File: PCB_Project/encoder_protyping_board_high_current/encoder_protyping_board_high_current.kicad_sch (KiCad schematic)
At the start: 15 parts, among them J1 Conn_01x08, J2 Conn_01x02_Pin, J3 Conn_01x04_Pin

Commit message: high current version done
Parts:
- JP1: footprint Jumper:SolderJumper-3_P1.3mm_Open_RoundedPad1.0x1.5mm -> Jumper:SolderJumper-3_P1.3mm_Open_RoundedPad1.0x1.5mm_NumberLabels
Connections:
- net GND: no longer J1.7 (Pin_7), U1.2 (P1)
- new net: J1.7 (Pin_7), U1.2 (P1)
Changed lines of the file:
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@@
-	)
-	(junction
-		(at 148.59 72.39)
-		(diameter 0)
-		(color 0 0 0 0)
 	)
 	(junction
@@
 	(wire
 		(pts
+			(xy 130.81 72.39) (xy 115.57 72.39)
+		)
+		(stroke
+			(width 0)
+			(type default)
+		)
+	)
+	(wire
+		(pts
 			(xy 182.88 115.57) (xy 166.37 115.57)
 		)
@@
 	(wire
 		(pts
-			(xy 158.75 64.77) (xy 215.9 64.77)
-		)
-		(stroke
-			(width 0)
-			(type default)
-		)
-	)
-	(wire
-		(pts
-			(xy 148.59 72.39) (xy 158.75 72.39)
-		)
-		(stroke
-			(width 0)
-			(type default)
-		)
-	)
-	(wire
-		(pts
 			(xy 74.93 83.82) (xy 92.71 83.82)
 		)
@@
 	(wire
 		(pts
+			(xy 115.57 69.85) (xy 129.54 69.85)
+		)
+		(stroke
+			(width 0)
+			(type default)
+		)
+	)
+	(wire
+		(pts
 			(xy 66.04 90.17) (xy 69.85 90.17)
 		)
@@
 	(wire
 		(pts
+			(xy 129.54 62.23) (xy 217.17 62.23)
+		)
+		(stroke
+			(width 0)
+			(type default)
+		)
+	)
+	(wire
+		(pts
 			(xy 148.59 120.65) (xy 143.51 120.65)
 		)
@@
 	(wire
 		(pts
-			(xy 115.57 72.39) (xy 148.59 72.39)
-		)
-		(stroke
-			(width 0)
-			(type default)
-		)
-	)
-	(wire
-		(pts
 			(xy 166.37 85.09) (xy 204.47 85.09)
 		)
@@
 	(wire
 		(pts
+			(xy 129.54 69.85) (xy 129.54 62.23)
+		)
+		(stroke
+			(width 0)
+			(type default)
+		)
+	)
+	(wire
+		(pts
 			(xy 74.93 86.36) (xy 92.71 86.36)
 		)
@@
 	(wire
 		(pts
-			(xy 158.75 72.39) (xy 158.75 64.77)
-		)
-		(stroke
-			(width 0)
-			(type default)
-		)
-	)
-	(wire
-		(pts
-			(xy 115.57 69.85) (xy 156.21 69.85)
+			(xy 130.81 64.77) (xy 130.81 72.39)
 		)
 		(stroke
@@
 	(wire
 		(pts
-			(xy 156.21 62.23) (xy 217.17 62.23)
-		)
-		(stroke
-			(width 0)
-			(type default)
-		)
-	)
-	(wire
-		(pts
 			(xy 69.85 90.17) (xy 76.2 90.17)
 		)
@@
 	(wire
 		(pts
+			(xy 130.81 64.77) (xy 215.9 64.77)
+		)
+		(stroke
+			(width 0)
+			(type default)
+		)
+	)
+	(wire
+		(pts
 			(xy 173.99 90.17) (xy 166.37 90.17)
 		)
@@
 		(pts
 			(xy 215.9 64.77) (xy 215.9 107.95)
-		)
-		(stroke
-			(width 0)
-			(type default)
-		)
-	)
-	(wire
-		(pts
-			(xy 156.21 69.85) (xy 156.21 62.23)
 		)
 		(stroke
@@
 			)
 		)
-		(property "Footprint" "Jumper:SolderJumper-3_P1.3mm_Open_RoundedPad1.0x1.5mm"
+		(property "Footprint" "Jumper:SolderJumper-3_P1.3mm_Open_RoundedPad1.0x1.5mm_NumberLabels"
 			(at 74.93 71.12 0)
 			(effects
@@
 	(symbol
 		(lib_id "power:GND")
-		(at 148.59 72.39 180)
+		(at 148.59 72.39 90)
 		(unit 1)
 		(exclude_from_sim no)
@@
 		(fields_autoplaced yes)
 		(property "Reference" "#PWR014"
-			(at 148.59 66.04 0)
+			(at 154.94 72.39 0)
 			(effects
 				(font
@@
 		)
 		(property "Value" "GND"
-			(at 148.59 67.31 0)
-			(effects
-				(font
-					(size 1.27 1.27)
-				)
-			)
-		)
+			(at 152.4 72.3899 90)
+			(effects
+				(font
+					(size 1.27 1.27)
+				)
+				(justify right)
+			)
+		)

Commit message: pin headers not pin sockets
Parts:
- J1: footprint Connector_PinSocket_2.54mm:PinSocket_1x08_P2.54mm_Vertical -> Connector_PinHeader_2.54mm:PinHeader_1x08_P2.54mm_Vertical
- J3: footprint Connector_PinSocket_2.54mm:PinSocket_1x04_P2.54mm_Vertical -> Connector_PinHeader_2.54mm:PinHeader_1x04_P2.54mm_Vertical
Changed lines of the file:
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@@
 			)
 		)
-		(property "Footprint" "Connector_PinSocket_2.54mm:PinSocket_1x04_P2.54mm_Vertical"
+		(property "Footprint" "Connector_PinHeader_2.54mm:PinHeader_1x04_P2.54mm_Vertical"
 			(at 88.9 41.91 0)
 			(effects
@@
 			)
 		)
-		(property "Footprint" "Connector_PinSocket_2.54mm:PinSocket_1x08_P2.54mm_Vertical"
+		(property "Footprint" "Connector_PinHeader_2.54mm:PinHeader_1x08_P2.54mm_Vertical"
 			(at 209.55 90.17 0)
 			(effects

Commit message: fixes
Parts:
- renumbered J2 to J1, J3 to J2, J1 to J3, JP2 to JP1, JP1 to JP2, R2 to R1, R3 to R2, R1 to R3
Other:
- moved on the sheet: R3

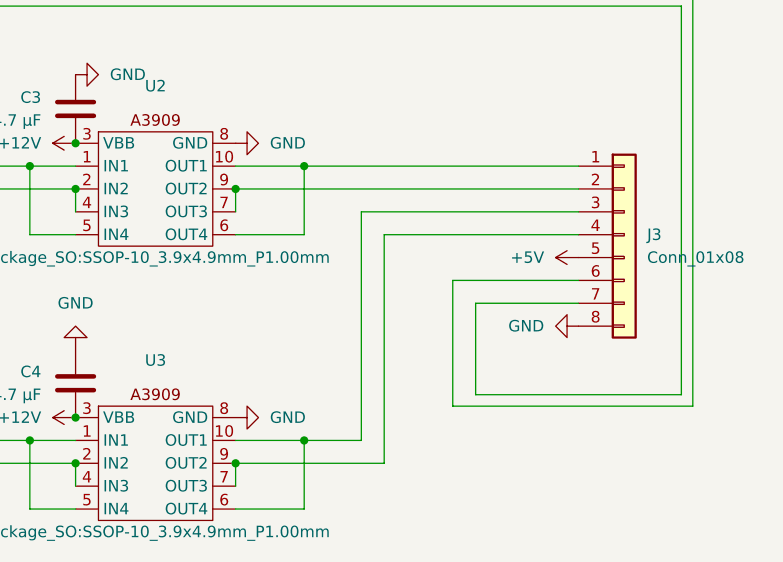
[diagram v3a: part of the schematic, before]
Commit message: finaly did that change to make it so this board could run with just a single chip
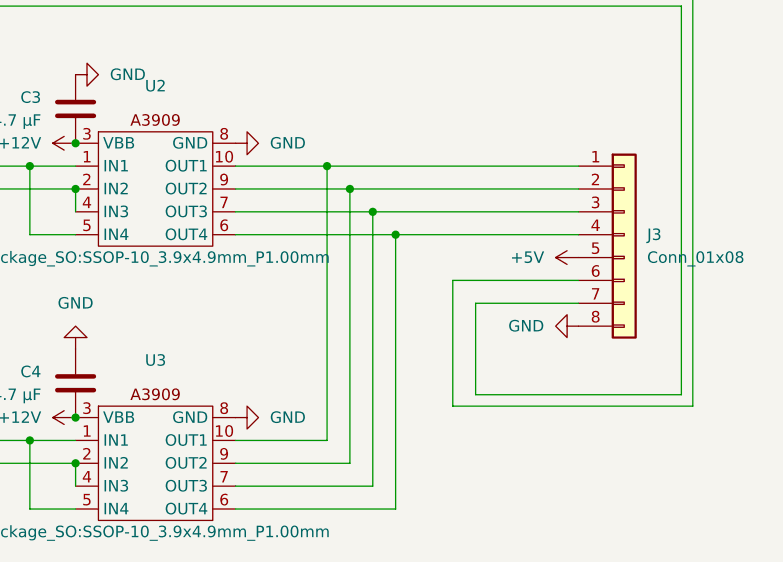
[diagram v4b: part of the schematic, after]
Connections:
- net at J3.1 (Pin_1), U2.10 (OUT1): now also U3.10 (OUT1); no longer U2.6 (OUT4)
- net at J3.2 (Pin_2), U2.9 (OUT2): now also U3.9 (OUT2); no longer U2.7 (OUT3)
- new net: J3.3 (Pin_3), U2.7 (OUT3), U3.7 (OUT3)
- new net: J3.4 (Pin_4), U2.6 (OUT4), U3.6 (OUT4)
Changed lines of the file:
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@@
+	)
+	(junction
+		(at 184.15 90.17)
+		(diameter 0)
+		(color 0 0 0 0)
+	)
+	(junction
+		(at 179.07 85.09)
+		(diameter 0)
+		(color 0 0 0 0)
 	)
 	(junction
@@
 	)
 	(junction
-		(at 166.37 85.09)
-		(diameter 0)
-		(color 0 0 0 0)
-	)
-	(junction
 		(at 143.51 113.03)
 		(diameter 0)
@@
 	)
 	(junction
+		(at 176.53 82.55)
+		(diameter 0)
+		(color 0 0 0 0)
+	)
+	(junction
 		(at 148.59 115.57)
 		(diameter 0)
@@
 	)
 	(junction
-		(at 173.99 113.03)
-		(diameter 0)
-		(color 0 0 0 0)
-	)
-	(junction
-		(at 173.99 82.55)
-		(diameter 0)
-		(color 0 0 0 0)
-	)
-	(junction
-		(at 166.37 115.57)
+		(at 181.61 87.63)
 		(diameter 0)
 		(color 0 0 0 0)
@@
 	(wire
 		(pts
+			(xy 184.15 90.17) (xy 184.15 120.65)
+		)
+		(stroke
+			(width 0)
+			(type default)
+		)
+	)
+	(wire
+		(pts
 			(xy 143.51 113.03) (xy 148.59 113.03)
 		)
@@
 	(wire
 		(pts
-			(xy 180.34 113.03) (xy 180.34 87.63)
+			(xy 179.07 115.57) (xy 166.37 115.57)
 		)
 		(stroke
@@
 	(wire
 		(pts
-			(xy 166.37 82.55) (xy 173.99 82.55)
-		)
-		(stroke
-			(width 0)
-			(type default)
-		)
-	)
-	(wire
-		(pts
-			(xy 166.37 85.09) (xy 166.37 87.63)
-		)
-		(stroke
-			(width 0)
-			(type default)
-		)
-	)
-	(wire
-		(pts
 			(xy 115.57 87.63) (xy 133.35 87.63)
 		)
@@
 	(wire
 		(pts
-			(xy 182.88 115.57) (xy 166.37 115.57)
-		)
-		(stroke
-			(width 0)
-			(type default)
-		)
-	)
-	(wire
-		(pts
 			(xy 91.44 76.2) (xy 92.71 76.2)
 		)
@@
 	(wire
 		(pts
-			(xy 180.34 87.63) (xy 204.47 87.63)
+			(xy 166.37 87.63) (xy 181.61 87.63)
+		)
+		(stroke
+			(width 0)
+			(type default)
+		)
+	)
+	(wire
+		(pts
+			(xy 176.53 82.55) (xy 176.53 113.03)
 		)
 		(stroke
@@
 	(wire
 		(pts
+			(xy 166.37 90.17) (xy 184.15 90.17)
+		)
+		(stroke
+			(width 0)
+			(type default)
+		)
+	)
+	(wire
+		(pts
+			(xy 166.37 118.11) (xy 181.61 118.11)
+		)
+		(stroke
+			(width 0)
+			(type default)
+		)
+	)
+	(wire
+		(pts
 			(xy 190.5 95.25) (xy 204.47 95.25)
 		)
@@
 	(wire
 		(pts
+			(xy 166.37 120.65) (xy 184.15 120.65)
+		)
+		(stroke
+			(width 0)
+			(type default)
+		)
+	)
+	(wire
+		(pts
 			(xy 115.57 90.17) (xy 130.81 90.17)
 		)
@@
 	(wire
 		(pts
+			(xy 181.61 87.63) (xy 181.61 118.11)
+		)
+		(stroke
+			(width 0)
+			(type default)
+		)
+	)
+	(wire
+		(pts
 			(xy 129.54 62.23) (xy 217.17 62.23)
 		)
@@
 	(wire
 		(pts
-			(xy 182.88 90.17) (xy 182.88 115.57)
+			(xy 166.37 82.55) (xy 176.53 82.55)
 		)
 		(stroke
@@
 	(wire
 		(pts
-			(xy 166.37 85.09) (xy 204.47 85.09)
+			(xy 179.07 85.09) (xy 179.07 115.57)
 		)
 		(stroke
@@
 	(wire
 		(pts
-			(xy 173.99 113.03) (xy 173.99 120.65)
+			(xy 181.61 87.63) (xy 204.47 87.63)
 		)
 		(stroke
@@
 	(wire
 		(pts
-			(xy 173.99 113.03) (xy 180.34 113.03)
-		)
-		(stroke
-			(width 0)
-			(type default)
-		)
-	)
-	(wire
-		(pts
 			(xy 148.59 82.55) (xy 143.51 82.55)
 		)
@@
 	(wire
 		(pts
-			(xy 173.99 82.55) (xy 173.99 90.17)
-		)
-		(stroke
-			(width 0)
-			(type default)
-		)
-	)
-	(wire
-		(pts
-			(xy 166.37 120.65) (xy 173.99 120.65)
-		)
-		(stroke
-			(width 0)
-			(type default)
-		)
-	)
-	(wire
-		(pts
 			(xy 143.51 120.65) (xy 143.51 113.03)
 		)
@@
 	(wire
 		(pts
+			(xy 184.15 90.17) (xy 204.47 90.17)
+		)
+		(stroke
+			(width 0)
+			(type default)
+		)
+	)
+	(wire
+		(pts
 			(xy 69.85 90.17) (xy 76.2 90.17)
 		)
@@
 	(wire
 		(pts
-			(xy 173.99 82.55) (xy 204.47 82.55)
+			(xy 176.53 82.55) (xy 204.47 82.55)
 		)
 		(stroke
@@
 	(wire
 		(pts
-			(xy 173.99 90.17) (xy 166.37 90.17)
+			(xy 176.53 113.03) (xy 166.37 113.03)
 		)
 		(stroke
@@
 	(wire
 		(pts
-			(xy 166.37 115.57) (xy 166.37 118.11)
-		)
-		(stroke
-			(width 0)
-			(type default)
-		)
-	)
-	(wire
-		(pts
-			(xy 166.37 113.03) (xy 173.99 113.03)
-		)
-		(stroke
-			(width 0)
-			(type default)
-		)
-	)
-	(wire
-		(pts
-			(xy 204.47 90.17) (xy 182.88 90.17)
-		)
-		(stroke
+			(xy 166.37 85.09) (xy 179.07 85.09)
+		)
+		(stroke
+			(width 0)
+			(type default)
+		)
+	)
+	(wire
+		(pts
+			(xy 179.07 85.09) (xy 204.47 85.09)
+		)
+		(stroke

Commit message: that would have been bad
changed the outputs to the chips but not the inputs
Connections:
- net at U1.12 (OUT0), U2.1 (IN1): now also U3.1 (IN1); no longer U2.5 (IN4)
- net at U1.11 (OUT1), U2.2 (IN2): now also U3.2 (IN2); no longer U2.4 (IN3)
- new net: U1.10 (OUT2), U2.4 (IN3), U3.4 (IN3)
- new net: U1.9 (OUT3), U2.5 (IN4), U3.5 (IN4)
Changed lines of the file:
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@@
 	(paper "A4")
 	(junction
-		(at 143.51 82.55)
-		(diameter 0)
-		(color 0 0 0 0)
-	)
-	(junction
 		(at 184.15 90.17)
 		(diameter 0)
@@
 	)
 	(junction
+		(at 125.73 90.17)
+		(diameter 0)
+		(color 0 0 0 0)
+	)
+	(junction
 		(at 179.07 85.09)
 		(diameter 0)
@@
 	)
 	(junction
-		(at 143.51 113.03)
+		(at 128.27 87.63)
+		(diameter 0)
+		(color 0 0 0 0)
+	)
+	(junction
+		(at 133.35 82.55)
 		(diameter 0)
 		(color 0 0 0 0)
@@
 	)
 	(junction
-		(at 148.59 85.09)
-		(diameter 0)
-		(color 0 0 0 0)
-	)
-	(junction
 		(at 148.59 110.49)
 		(diameter 0)
@@
 	)
 	(junction
-		(at 148.59 115.57)
+		(at 130.81 85.09)
 		(diameter 0)
 		(color 0 0 0 0)
@@
 	(wire
 		(pts
-			(xy 143.51 113.03) (xy 148.59 113.03)
+			(xy 128.27 87.63) (xy 148.59 87.63)
 		)
 		(stroke
@@
 	(wire
 		(pts
-			(xy 115.57 85.09) (xy 148.59 85.09)
-		)
-		(stroke
-			(width 0)
-			(type default)
-		)
-	)
-	(wire
-		(pts
 			(xy 193.04 97.79) (xy 204.47 97.79)
 		)
@@
 	(wire
 		(pts
-			(xy 115.57 87.63) (xy 133.35 87.63)
-		)
-		(stroke
-			(width 0)
-			(type default)
-		)
-	)
-	(wire
-		(pts
-			(xy 130.81 90.17) (xy 130.81 115.57)
+			(xy 148.59 120.65) (xy 125.73 120.65)
+		)
+		(stroke
+			(width 0)
+			(type default)
+		)
+	)
+	(wire
+		(pts
+			(xy 130.81 115.57) (xy 148.59 115.57)
 		)
 		(stroke
@@
 	(wire
 		(pts
+			(xy 115.57 87.63) (xy 128.27 87.63)
+		)
+		(stroke
+			(width 0)
+			(type default)
+		)
+	)
+	(wire
+		(pts
 			(xy 36.83 68.58) (xy 43.18 68.58)
 		)
@@
 	(wire
 		(pts
+			(xy 128.27 118.11) (xy 148.59 118.11)
+		)
+		(stroke
+			(width 0)
+			(type default)
+		)
+	)
+	(wire
+		(pts
+			(xy 125.73 120.65) (xy 125.73 90.17)
+		)
+		(stroke
+			(width 0)
+			(type default)
+		)
+	)
+	(wire
+		(pts
 			(xy 166.37 87.63) (xy 181.61 87.63)
 		)
@@
 	(wire
 		(pts
+			(xy 130.81 85.09) (xy 130.81 115.57)
+		)
+		(stroke
+			(width 0)
+			(type default)
+		)
+	)
+	(wire
+		(pts
 			(xy 176.53 82.55) (xy 176.53 113.03)
 		)
@@
 	(wire
 		(pts
+			(xy 133.35 82.55) (xy 148.59 82.55)
+		)
+		(stroke
+			(width 0)
+			(type default)
+		)
+	)
+	(wire
+		(pts
 			(xy 43.18 66.04) (xy 36.83 66.04)
 		)
@@
 	(wire
 		(pts
+			(xy 115.57 85.09) (xy 130.81 85.09)
+		)
+		(stroke
+			(width 0)
+			(type default)
+		)
+	)
+	(wire
+		(pts
 			(xy 115.57 69.85) (xy 129.54 69.85)
 		)
@@
 	(wire
 		(pts
-			(xy 115.57 90.17) (xy 130.81 90.17)
-		)
-		(stroke
-			(width 0)
-			(type default)
-		)
-	)
-	(wire
-		(pts
-			(xy 130.81 115.57) (xy 148.59 115.57)
+			(xy 115.57 90.17) (xy 125.73 90.17)
+		)
+		(stroke
+			(width 0)
+			(type default)
+		)
+	)
+	(wire
+		(pts
+			(xy 130.81 85.09) (xy 148.59 85.09)
 		)
 		(stroke
@@
 	(wire
 		(pts
-			(xy 115.57 82.55) (xy 143.51 82.55)
+			(xy 125.73 90.17) (xy 148.59 90.17)
+		)
+		(stroke
+			(width 0)
+			(type default)
+		)
+	)
+	(wire
+		(pts
+			(xy 128.27 87.63) (xy 128.27 118.11)
 		)
 		(stroke
@@
 	(wire
 		(pts
-			(xy 148.59 120.65) (xy 143.51 120.65)
-		)
-		(stroke
-			(width 0)
-			(type default)
-		)
-	)
-	(wire
-		(pts
 			(xy 166.37 82.55) (xy 176.53 82.55)
 		)
@@
 	(wire
 		(pts
-			(xy 133.35 87.63) (xy 133.35 113.03)
-		)
-		(stroke
-			(width 0)
-			(type default)
-		)
-	)
-	(wire
-		(pts
 			(xy 76.2 90.17) (xy 92.71 90.17)
 		)
@@
 	(wire
 		(pts
-			(xy 143.51 90.17) (xy 148.59 90.17)
-		)
-		(stroke
-			(width 0)
-			(type default)
-		)
-	)
-	(wire
-		(pts
-			(xy 148.59 115.57) (xy 148.59 118.11)
-		)
-		(stroke
-			(width 0)
-			(type default)
-		)
-	)
-	(wire
-		(pts
 			(xy 49.53 66.04) (xy 43.18 66.04)
 		)
@@
 	(wire
 		(pts
-			(xy 148.59 85.09) (xy 148.59 87.63)
-		)
-		(stroke
-			(width 0)
-			(type default)
-		)
-	)
-	(wire
-		(pts
-			(xy 133.35 113.03) (xy 143.51 113.03)
-		)
-		(stroke
-			(width 0)
-			(type default)
-		)
-	)
-	(wire
-		(pts
 			(xy 181.61 87.63) (xy 204.47 87.63)
 		)
@@
 	(wire
 		(pts
-			(xy 143.51 82.55) (xy 143.51 90.17)
-		)
-		(stroke
-			(width 0)
-			(type default)
-		)
-	)
-	(wire
-		(pts
 			(xy 78.74 71.12) (xy 92.71 71.12)
 		)
@@
 	(wire
 		(pts
-			(xy 148.59 82.55) (xy 143.51 82.55)
-		)
-		(stroke
-			(width 0)
-			(type default)
-		)
-	)
-	(wire
-		(pts
 			(xy 129.54 69.85) (xy 129.54 62.23)
 		)
@@
 	(wire
 		(pts
+			(xy 133.35 113.03) (xy 148.59 113.03)
+		)
+		(stroke
+			(width 0)
+			(type default)
+		)
+	)
+	(wire
+		(pts
 			(xy 74.93 86.36) (xy 92.71 86.36)
 		)
@@
 	(wire
 		(pts
-			(xy 143.51 120.65) (xy 143.51 113.03)
-		)
-		(stroke
-			(width 0)
-			(type default)
-		)
-	)
-	(wire
-		(pts
 			(xy 184.15 90.17) (xy 204.47 90.17)
 		)
@@
 		)
 		(stroke
+			(width 0)
+			(type default)
+		)
+	)
+	(wire
+		(pts
+			(xy 115.57 82.55) (xy 133.35 82.55)
+		)
+		(stroke
+			(width 0)
+			(type default)
+		)
+	)
+	(wire
+		(pts
+			(xy 133.35 82.55) (xy 133.35 113.03)
+		)
+		(stroke
